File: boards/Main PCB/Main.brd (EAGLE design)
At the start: 101.6 x 76.2 mm, 91 parts, among them CN1 MINIB, CN2 MINIB, IC1 FT232RL, IC2 FT232RL, J1 3_PIN_JST-XH, J2 2_PIN_JST-XH, Q4 BSS138, Q5 BSS138, Q6 BSS138, Q7 BSS138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

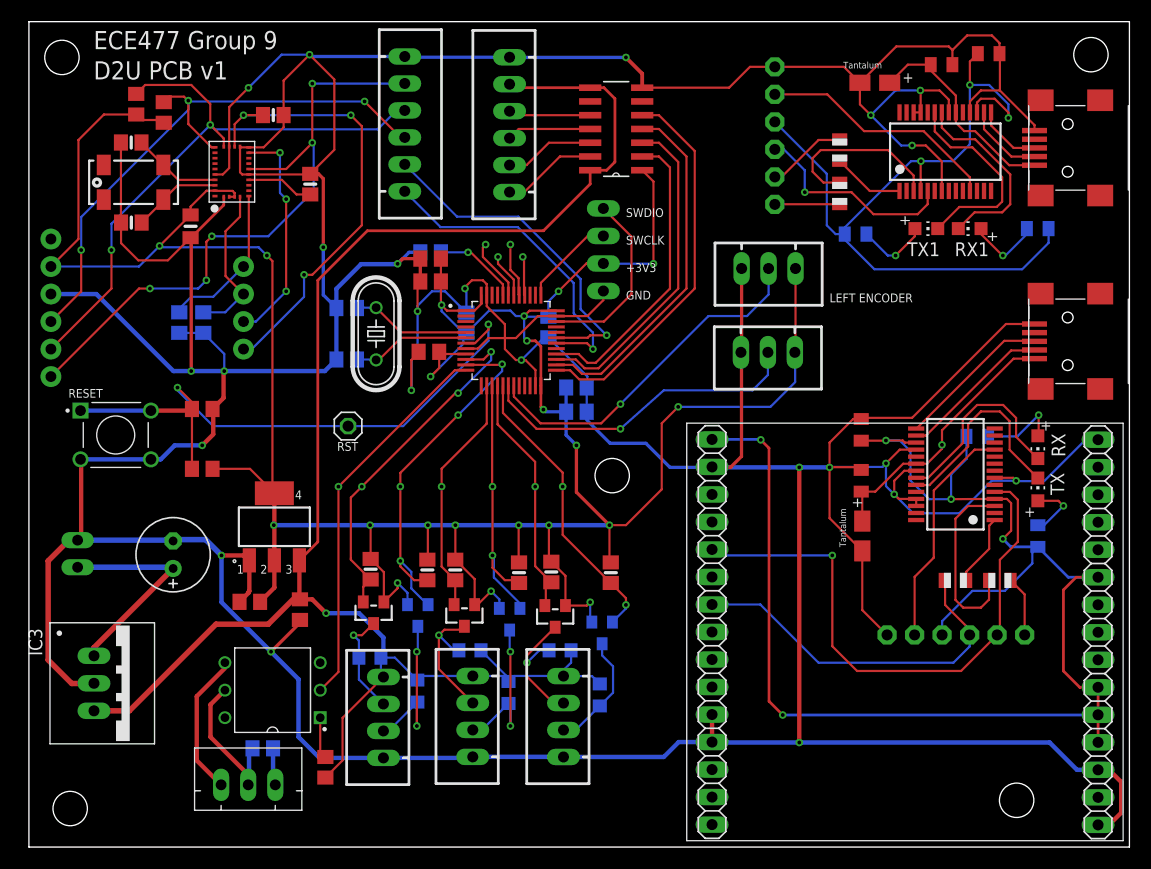
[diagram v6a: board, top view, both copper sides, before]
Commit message: Added indicator LEDs to board and cleaned up iOS assets
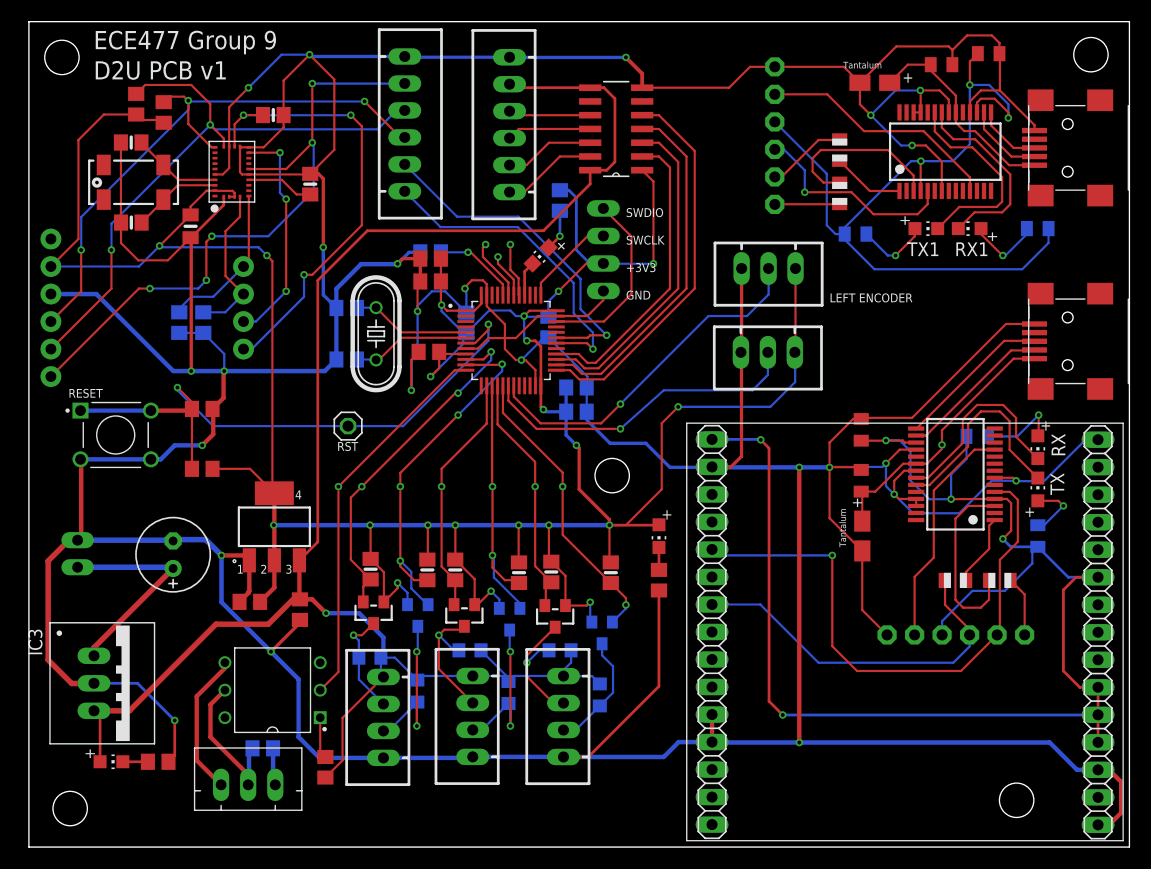
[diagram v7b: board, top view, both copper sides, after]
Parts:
- added R10, R11, R32: 1K, rcl:R0805
- added RX2, RX3, RX4: Green, adafruit:CHIP-LED0805
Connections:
- removed net TEST_GPIO4: U2.40
- new net N$12: R32.2, RX4.C
- new net N$13: RX2.C, U2.40
- new net N$3: R10.1, RX2.A
- new net N$4: R11.2, RX3.C
- net +3V3: now also R10.2, RX3.A
- net +5V: now also RX4.A
- net GND: now also R11.1, R32.1
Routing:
- net GND: track 668.3 -> 701.6 mm, vias 23 -> 24
- net +3V3: track 291.1 -> 305.3 mm
- net +5V: track 155.5 -> 160.4 mm
- net N$3: track 0.00 -> 3.82 mm, vias 0 -> 1
- net TEST_GPIO4: track 3.61 -> 0.00 mm, vias 1 -> 0
- net N$13: track 0.00 -> 3.23 mm
- net N$12: track 0.00 -> 2.32 mm
- net N$4: track 0.00 -> 2.06 mm
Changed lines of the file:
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@@
 <?xml version="1.0" encoding="utf-8"?>
 <!DOCTYPE eagle SYSTEM "eagle.dtd">
-<eagle version="9.3.1">
+<eagle version="9.3.0">
 <drawing>
 <settings>
@@
 <attribute name="VALUE" x="8.128" y="68.707" size="0.6096" layer="27" rot="R270"/>
 </element>
+<element name="R10" library="rcl" library_urn="urn:adsk.eagle:library:334" package="R0805" package3d_urn="urn:adsk.eagle:package:23553/2" value="1K" x="49.022" y="59.69" smashed="yes" rot="MR90">
+<attribute name="SPICEPREFIX" value="R" x="49.022" y="59.69" size="1.778" layer="28" rot="MR90" display="off"/>
+<attribute name="VALUE" x="47.244" y="59.054996875" size="0.8128" layer="28" rot="MR90"/>
+</element>
+<element name="RX2" library="adafruit" package="CHIP-LED0805" value="Green" x="47.244" y="54.61" smashed="yes" rot="R135"/>
+<element name="RX3" library="adafruit" package="CHIP-LED0805" value="Green" x="58.166" y="28.702" smashed="yes" rot="R180"/>
+<element name="R11" library="rcl" library_urn="urn:adsk.eagle:library:334" package="R0805" package3d_urn="urn:adsk.eagle:package:23553/2" value="1K" x="58.166" y="24.638" smashed="yes" rot="R90">
+<attribute name="SPICEPREFIX" value="R" x="58.166" y="24.638" size="1.778" layer="27" rot="R90" display="off"/>
+<attribute name="VALUE" x="60.198" y="24.003" size="0.8128" layer="27" rot="R90"/>
+</element>
+<element name="RX4" library="adafruit" package="CHIP-LED0805" value="Green" x="7.62" y="7.874" smashed="yes" rot="R270"/>
+<element name="R32" library="rcl" library_urn="urn:adsk.eagle:library:334" package="R0805" package3d_urn="urn:adsk.eagle:package:23553/2" value="1K" x="11.938" y="7.874" smashed="yes" rot="R180">
+<attribute name="SPICEPREFIX" value="R" x="11.938" y="7.874" size="1.778" layer="27" rot="R180" display="off"/>
+<attribute name="VALUE" x="12.573" y="10.16" size="1.27" layer="27" rot="R180"/>
+</element>
 </elements>
 <signals>
@@
 <wire x1="20.2876" y1="23.5563375" x2="20.2876" y2="23.4816" width="0.4064" layer="1"/>
 <wire x1="20.2876" y1="23.4816" x2="19.444" y2="22.638" width="0.4064" layer="1"/>
+<contactref element="R11" pad="1"/>
+<contactref element="R32" pad="1"/>
+<wire x1="12.888" y1="7.874" x2="13.462" y2="8.448" width="0.254" layer="1"/>
+<wire x1="13.462" y1="8.448" x2="13.462" y2="11.684" width="0.254" layer="1"/>
+<via x="13.462" y="11.684" extent="1-16" drill="0.35"/>
+<wire x1="13.462" y1="11.684" x2="10.028" y2="15.118" width="0.254" layer="16"/>
+<wire x1="10.028" y1="15.118" x2="6.008" y2="15.118" width="0.254" layer="16"/>
+<wire x1="58.166" y1="23.688" x2="58.166" y2="14.8442" width="0.254" layer="1"/>
+<wire x1="58.166" y1="14.8442" x2="51.638" y2="8.3162" width="0.254" layer="1"/>
+<wire x1="51.638" y1="8.3162" x2="49.352" y2="8.3162" width="0.254" layer="1"/>
 </signal>
 <signal name="D+_GPS">
@@
 <wire x1="57.658" y1="53.848" x2="53.06" y2="53.848" width="0.2032" layer="16"/>
 <wire x1="53.06" y1="53.848" x2="53.032" y2="53.876" width="0.2032" layer="16"/>
-<wire x1="53.594" y1="29.718" x2="50.546" y2="32.766" width="0.3048" layer="1"/>
-<wire x1="50.546" y1="32.766" x2="50.546" y2="37.084" width="0.3048" layer="1"/>
+<wire x1="53.594" y1="29.718" x2="53.594" y2="30.226" width="0.3048" layer="1"/>
+<wire x1="53.594" y1="30.226" x2="50.8" y2="33.02" width="0.3048" layer="1"/>
+<wire x1="50.8" y1="36.83" x2="50.546" y2="37.084" width="0.3048" layer="1"/>
+<wire x1="50.8" y1="36.83" x2="50.8" y2="33.02" width="0.3048" layer="1"/>
 <via x="50.546" y="37.084" extent="1-16" drill="0.35"/>
 <wire x1="49.596" y1="38.034" x2="49.596" y2="40.188" width="0.3048" layer="16"/>
@@
 <wire x1="9.906" y1="67.63" x2="6.924" y2="67.63" width="0.2032" layer="1"/>
 <wire x1="6.924" y1="67.63" x2="4.572" y2="65.278" width="0.2032" layer="1"/>
+<contactref element="RX3" pad="A"/>
+<contactref element="R10" pad="2"/>
+<wire x1="49.022" y1="60.64" x2="49.85" y2="60.64" width="0.254" layer="16"/>
+<wire x1="49.85" y1="60.64" x2="50.546" y2="59.944" width="0.254" layer="16"/>
+<wire x1="50.546" y1="59.944" x2="50.546" y2="55.118" width="0.254" layer="16"/>
+<wire x1="50.546" y1="55.118" x2="51.816" y2="53.848" width="0.254" layer="16"/>
+<wire x1="51.816" y1="53.848" x2="53.06" y2="53.848" width="0.254" layer="16"/>
+<wire x1="58.166" y1="29.752" x2="58.132" y2="29.718" width="0.254" layer="1"/>
+<wire x1="58.132" y1="29.718" x2="53.594" y2="29.718" width="0.254" layer="1"/>
 </signal>
 <signal name="N$6">
@@
 <wire x1="51.816" y1="70.104" x2="44.6958" y2="70.104" width="0.254" layer="1"/>
 <wire x1="44.6958" y1="70.104" x2="44.374" y2="70.4258" width="0.254" layer="1"/>
+<contactref element="RX4" pad="A"/>
+<wire x1="6.57" y1="7.874" x2="6.57" y2="12.016" width="0.254" layer="1"/>
+<wire x1="6.57" y1="12.016" x2="6.008" y2="12.578" width="0.254" layer="1"/>
 </signal>
 <signal name="N$5">
@@
 <wire x1="45.2088" y1="52.5209375" x2="44.45" y2="53.2797375" width="0.2032" layer="1"/>
 </signal>
-<signal name="TEST_GPIO4">
-<contactref element="U2" pad="40"/>
-<via x="45.593" y="54.483" extent="1-16" drill="0.35"/>
-<wire x1="45.764" y1="50.948" x2="45.7088" y2="51.0032" width="0.2032" layer="1"/>
-<wire x1="45.7088" y1="51.0032" x2="45.7088" y2="54.373675" width="0.2032" layer="1"/>
-<wire x1="45.7088" y1="54.373675" x2="45.599475" y2="54.483" width="0.2032" layer="1"/>
-<wire x1="45.593" y1="54.483" x2="45.599475" y2="54.483" width="0.2032" layer="1"/>
-</signal>
 <signal name="N$59">
 <contactref element="JP5" pad="1"/>
 </signal>
+<signal name="N$4">
+<contactref element="RX3" pad="C"/>
+<contactref element="R11" pad="2"/>
+<wire x1="58.166" y1="27.652" x2="58.166" y2="25.588" width="0.254" layer="1"/>
+</signal>
+<signal name="N$12">
+<contactref element="R32" pad="2"/>
+<contactref element="RX4" pad="C"/>
+<wire x1="8.67" y1="7.874" x2="10.988" y2="7.874" width="0.254" layer="1"/>
+</signal>
+<signal name="N$3">
+<contactref element="R10" pad="1"/>
+<contactref element="RX2" pad="A"/>
+<via x="49.022" y="56.388" extent="1-16" drill="0.35"/>
+<wire x1="47.986459375" y1="55.352459375" x2="49.022" y2="56.388" width="0.254" layer="1"/>
+<wire x1="49.022" y1="56.388" x2="49.022" y2="58.74" width="0.254" layer="16"/>
+</signal>
+<signal name="N$13">
+<contactref element="RX2" pad="C"/>
+<contactref element="U2" pad="40"/>
+<wire x1="46.5015375" y1="53.8675375" x2="45.764" y2="53.13" width="0.254" layer="1"/>
+<wire x1="45.764" y1="53.13" x2="45.764" y2="50.948" width="0.254" layer="1"/>
+</signal>
 </signals>

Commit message: Cleaning up routing and labels for design review
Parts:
- R10, R11, R13, R14, R2, R3: value 1K -> 47
- R32: value 1K -> 100
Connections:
- net ENCODER1 renamed ADC_CH8
- net ENCODER2 renamed ADC_CH9
- net N$24 renamed SWDIO
- net N$28 renamed SWCLK
- net N$30 renamed SPI2_NSS_3V3
- net N$31 renamed SPI2_SCK_3V3
- net N$32 renamed SPI2_MISO_3V3
- net N$33 renamed SPI2_MOSI_3V3
- net N$35 renamed TX_JETSON
- net N$39 renamed RX_JETSON
- net N$47 renamed MOSI_5V
- net N$51 renamed MISO_5V
- net N$52 renamed SCK_5V
- net N$53 renamed NSS_5V
- removed net N$59: JP5.1
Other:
- board text added: "12V IN"
- board text added: "12V TO 5V SWR"
- board text added: "FT232RL"
- board text added: "Keith Aylwin"
- board text added: "Luke Armbruster"
- board text added: "MC S1"
- board text added: "Michael Karrs"
- board text added: "Troy Conlin"
